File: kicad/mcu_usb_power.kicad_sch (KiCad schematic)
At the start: 41 parts, among them J2 USB4105-GF-A, U7 MCXN947VDFT, U8 PCMF1USB3SZ

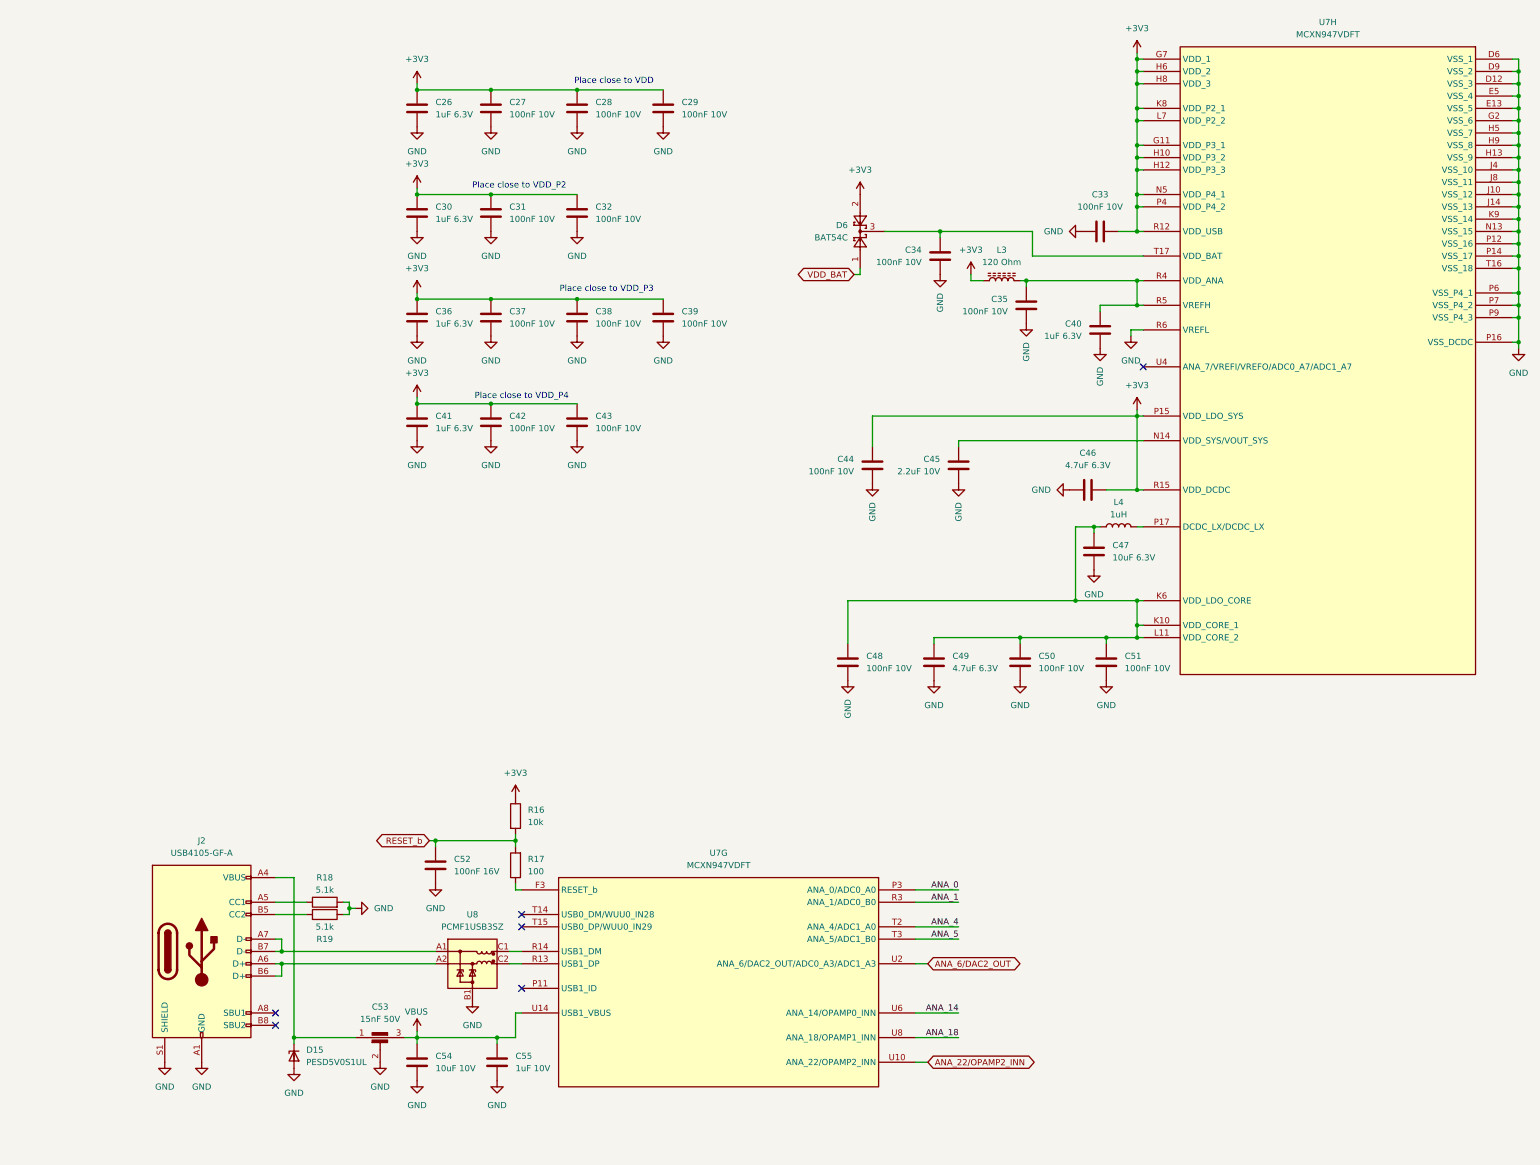
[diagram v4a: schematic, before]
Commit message: Updated schematic after feedback from Jari
- Finished schematic after feedback from Jari. It is at a finished state, can be reviewed by whole team now.
- Layouted MCXN with decoupling caps.
- Layouted Base100-T1 ethernet phy.
- Layouted the power supply a bit.
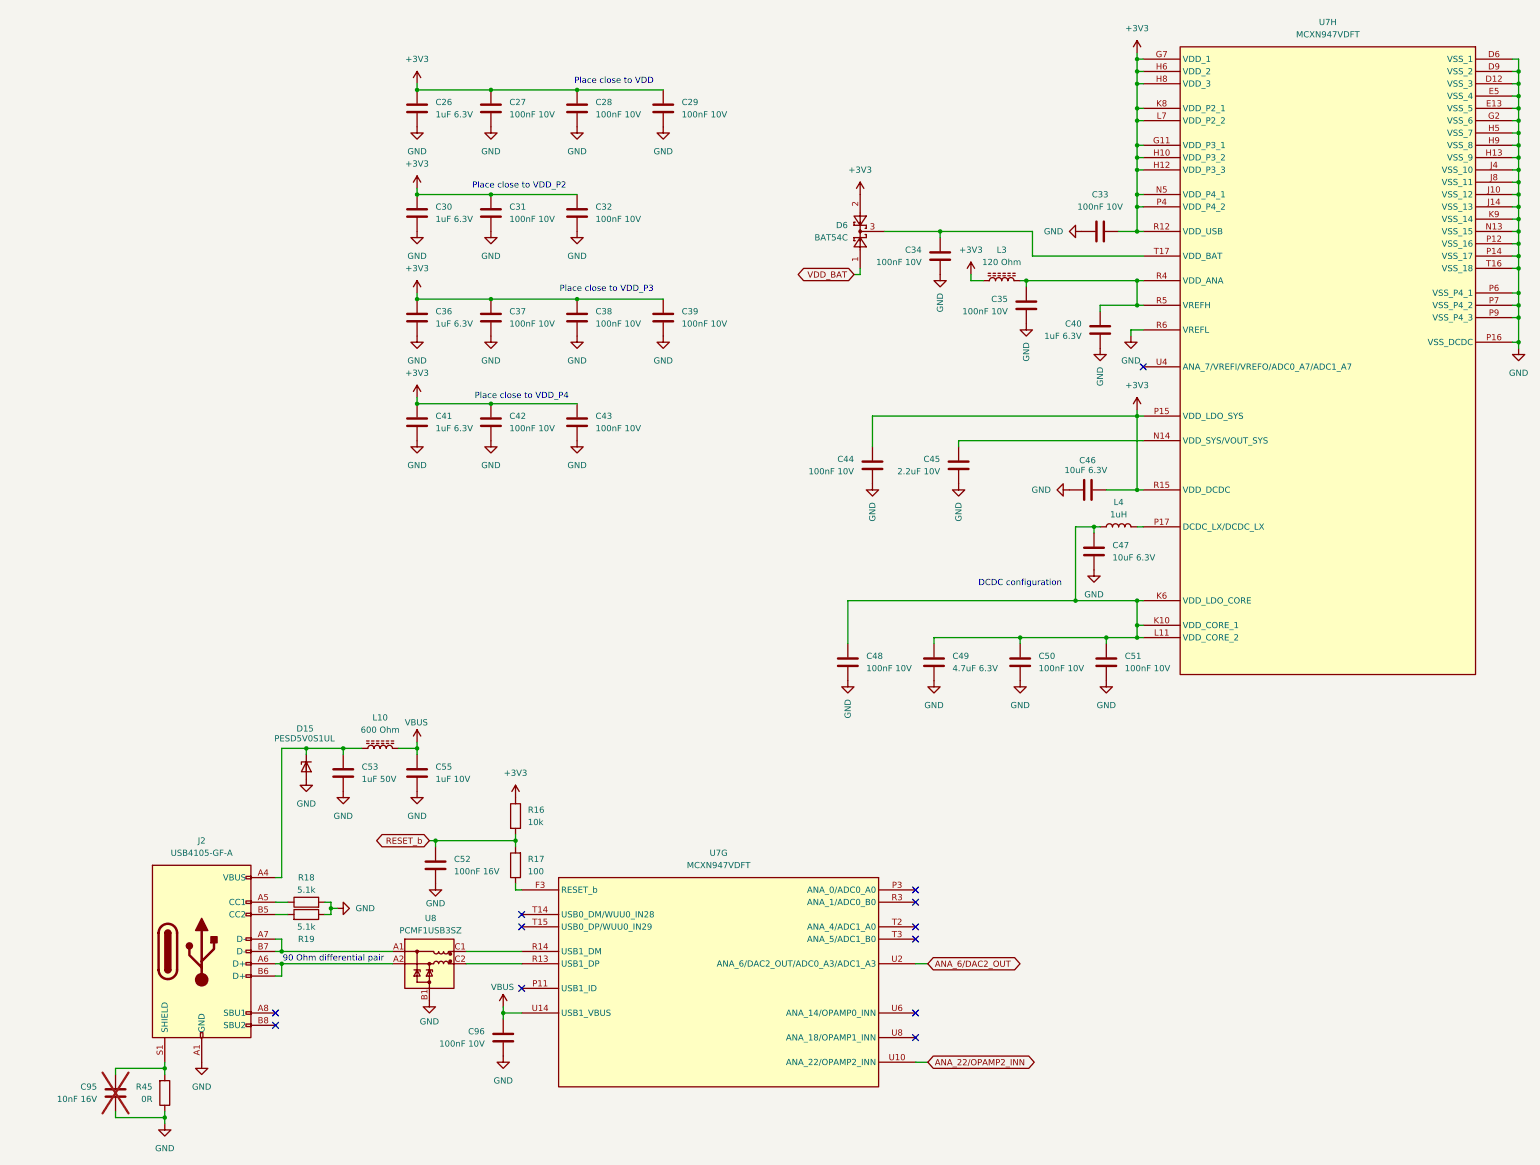
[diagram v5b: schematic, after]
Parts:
- removed C53: 15nF 50V, Capacitors:NFM31HK103R1H3L, symbol Capacitors:NFM31KC153R1H3L
- removed C54: 10uF 10V, Capacitor_SMD:C_0805_2012Metric, symbol Device:C
- added C53: 1uF 50V, Capacitor_SMD:C_0805_2012Metric, symbol Device:C
- added C95: 10nF 16V, symbol Device:C
- added C96: 100nF 10V, Capacitor_SMD:C_0201_0603Metric, symbol Device:C
- added L10: 600 Ohm, Inductor_SMD:L_0402_1005Metric, symbol Device:L_Ferrite
- added R45: 0R, symbol Device:R
- C46: value 4.7uF 6.3V -> 10uF 6.3V; MF Samsung Electro-Mechanics -> Murata Electronics; MFPN CL10B475KQ8NQNC -> GRM188Z71A106KA73D; Supplier PN C107368 -> C2959727
- C55: footprint Capacitor_SMD:C_0603_1608Metric -> Capacitor_SMD:C_0402_1005Metric; MF Samsung Electro-Mechanics -> Murata Electronics; MFPN CL10B105KA8NNNC -> GRM155Z71A105KE01D; Supplier PN C29936 -> C528974
- D15: MF (none) -> Nexperia; MFPN (none) -> PESD5V0S1UL,315; Supplier (none) -> JLCPCB; Supplier PN (none) -> C85402
- J2: MF Korean Hroparts Elec -> Korean Hroparts Elec
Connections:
- net +3V3: now also C46.2; no longer C46.1
- net GND: now also C46.1, C53.2, C95.2, C96.1, R45.1; no longer C46.2, J2.S1 (SHIELD)
- net VBUS: now also C96.2, L10.2
- net at D15.1 (K1), J2.A4 (VBUS), J2.A9 (VBUS)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: now also C53.1, L10.1
- net ANA_0: no longer names the net of U7.P3 (ANA_0/ADC0_A0)
- net ANA_1: no longer names the net of U7.R3 (ANA_1/ADC0_B0)
- net ANA_14: no longer names the net of U7.U6 (ANA_14/OPAMP0_INN)
- net ANA_18: no longer names the net of U7.U8 (ANA_18/OPAMP1_INN)
- net ANA_4: no longer names the net of U7.T2 (ANA_4/ADC1_A0)
- net ANA_5: no longer names the net of U7.T3 (ANA_5/ADC1_B0)
- new net: C95.1, J2.S1 (SHIELD), R45.2
- no-connect marks 6 -> 12
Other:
- note added: "90 Ohm differential pair"
- note added: "DCDC configuration"
- title: MR-MCXN-T1 Sensor hub -> MR-MCXN-T1 Sensor Node
- moved on the sheet: C55, D15, R18, R19, U8

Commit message: Finished schematic. Completed power and ENET phy layout.
Layouted power supply and ethernet phy around input connector.
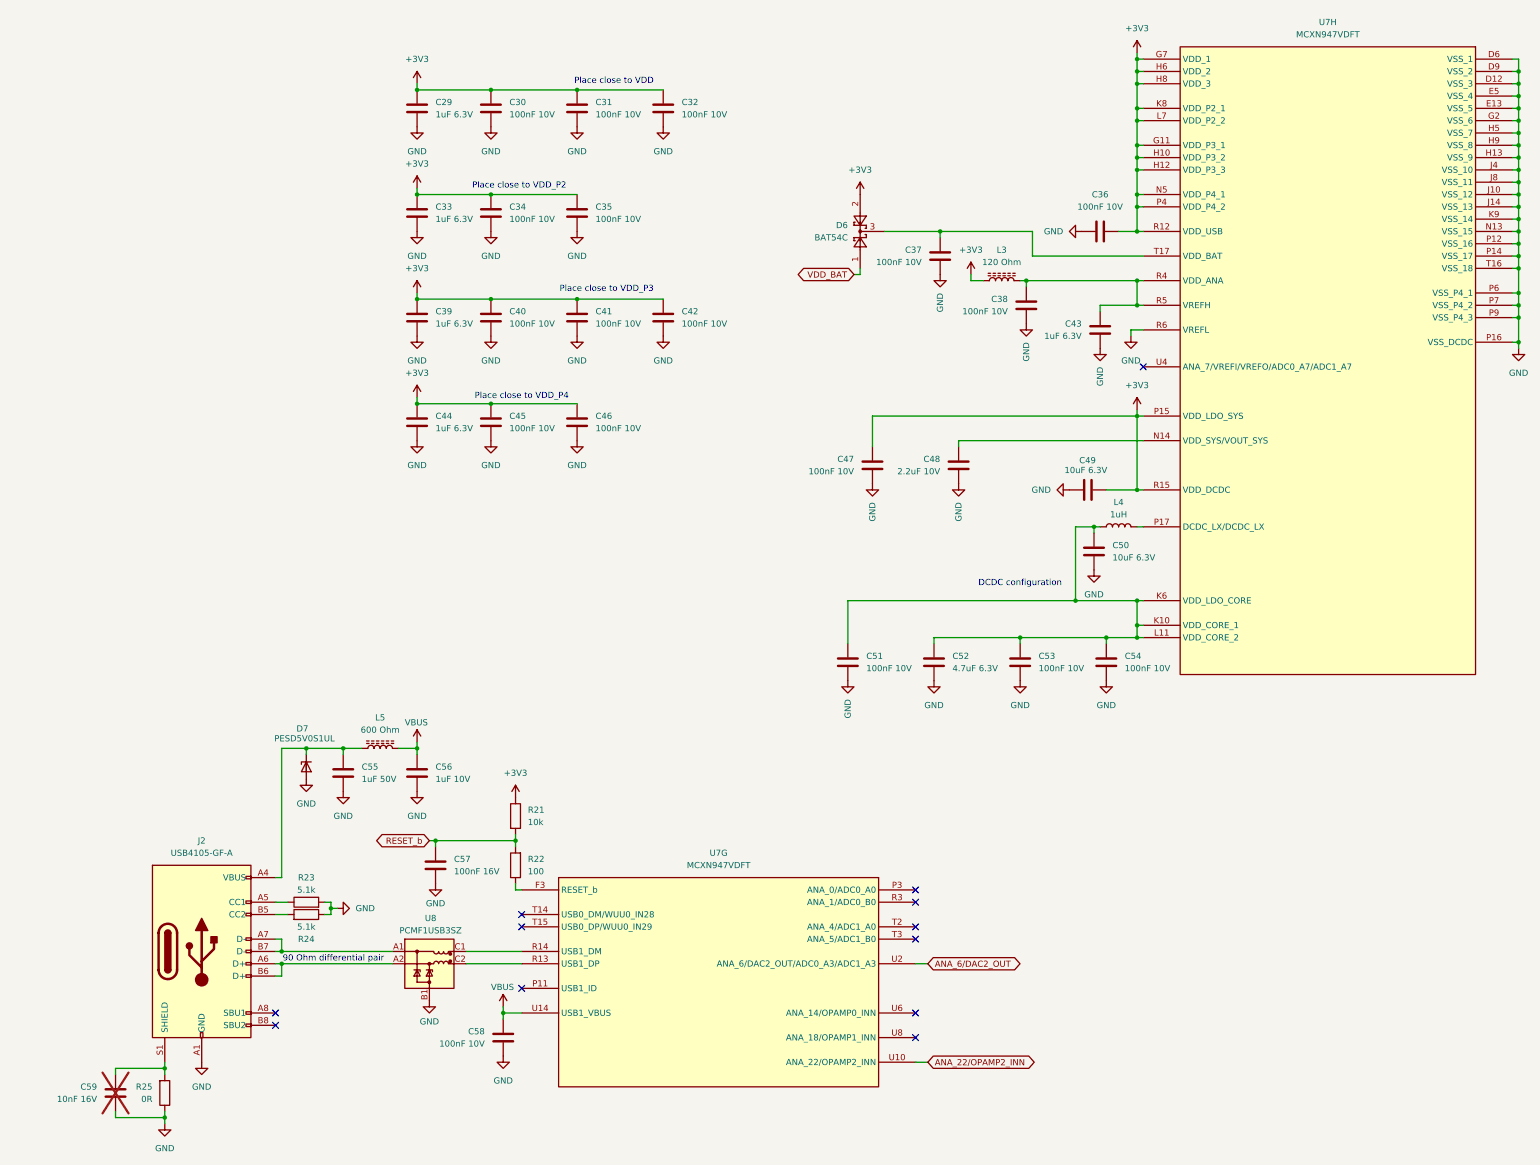
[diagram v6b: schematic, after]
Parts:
- C59: renamed from C95; footprint (none) -> Capacitor_SMD:C_0402_1005Metric; MF (none) -> Murata Electronics; MFPN (none) -> GRM155R71H103KA88D; Supplier (none) -> JLCPCB; Supplier PN (none) -> C77019
- R25: renamed from R45; footprint (none) -> Resistor_SMD:R_0402_1005Metric; MF (none) -> YAGEO; MFPN (none) -> RC0402JR-070RL; Supplier (none) -> JLCPCB; Supplier PN (none) -> C60485
- renumbered C26 to C29, C27 to C30, C28 to C31, C29 to C32, C30 to C33, C31 to C34, C32 to C35, C33 to C36, C34 to C37, C35 to C38, C36 to C39, C37 to C40, C38 to C41, C39 to C42, C40 to C43, C41 to C44, C42 to C45, C43 to C46, C44 to C47, C45 to C48, C46 to C49, C47 to C50, C48 to C51, C49 to C52, C50 to C53, C51 to C54, C53 to C55, C55 to C56, C52 to C57, C96 to C58, D15 to D7, L10 to L5, R16 to R21, R17 to R22, R18 to R23, R19 to R24

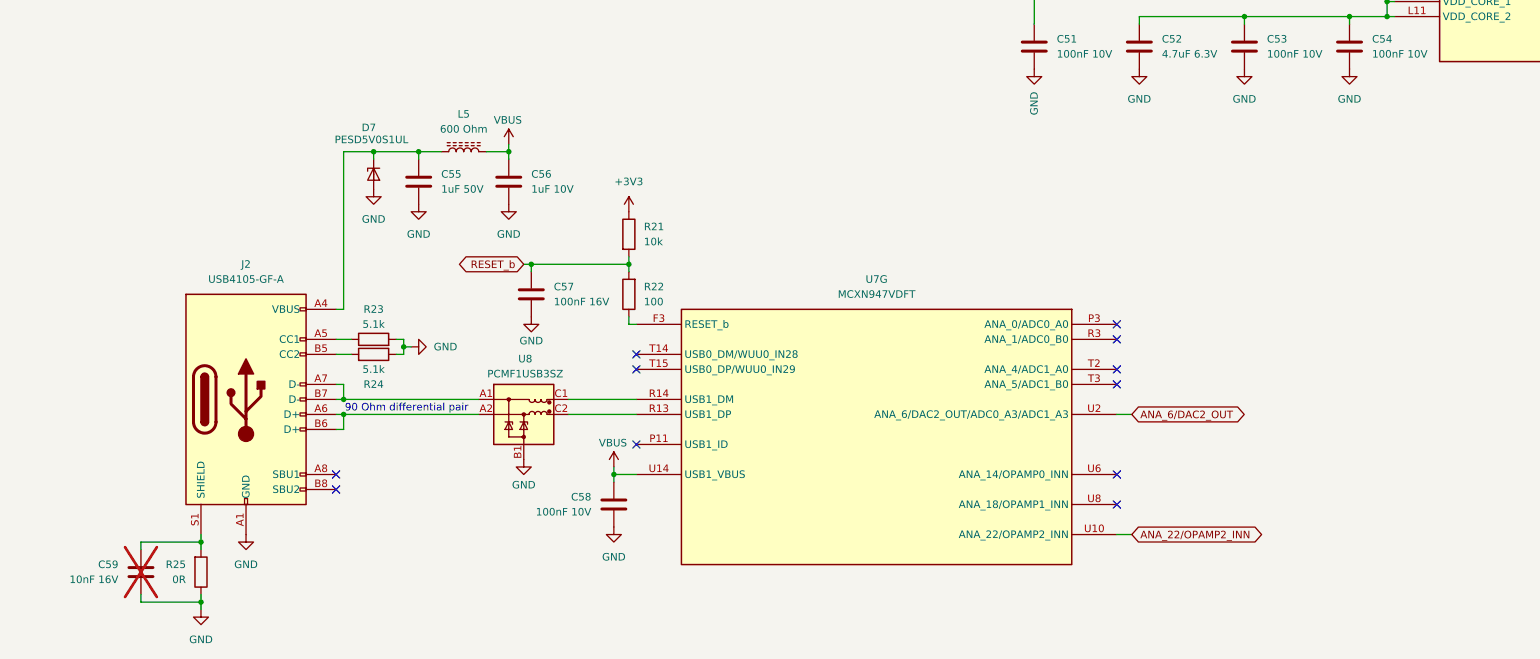
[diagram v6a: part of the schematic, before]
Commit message: Updated PCB layout
Implemented feedback:
- Placed ENET LEDs next to each other
- Added solder pads to output of RGB LED
- Made hole to hole distance in X-axis to 30.5mm
- Placed IMU a bit closer to the middle to still comply to the design rules by TDK.
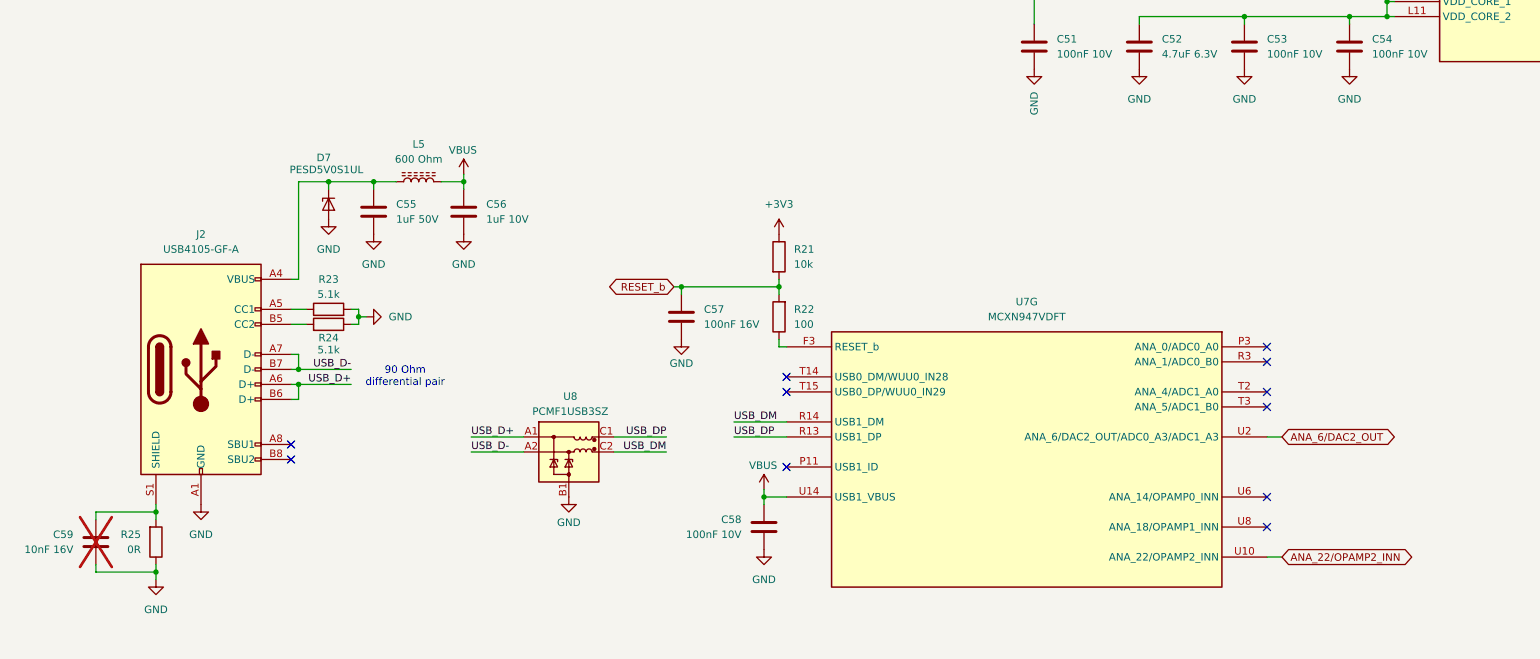
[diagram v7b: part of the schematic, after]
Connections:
- net USB_DM: now reaches U8.C2 (CH1_OUT-)
- net USB_DM: now also U7.R14 (USB1_DM); no longer U7.R13 (USB1_DP)
- net USB_DP: now reaches U8.C1 (CH1_OUT+)
- net USB_DP: now also U7.R13 (USB1_DP); no longer U7.R14 (USB1_DM)
- net USB_D-: now reaches J2.A7 (D-), J2.B7 (D-)
- net USB_D-: now also U8.A2 (CH1_IN-); no longer U8.A1 (CH1_IN+)
- net USB_D+: now reaches J2.A6 (D+), J2.B6 (D+)
- net USB_D+: now also U8.A1 (CH1_IN+); no longer U8.A2 (CH1_IN-)
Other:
- moved on the sheet: C55, C56, C57, C58, C59, D7, J2, L5, R21, R22, R23, R24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

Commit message: Updated layout and BOM
- Flipped Magnetometer so it is aligned with the axis of the IMU.
- Updated BOM so all parts can be sourced from DigiKey. Also added a row for JLCPCB part numbers if applicable.
- Replaced ISP button with the NanoT160AS. Added "ISP" in silkscreen at that button.
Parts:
- C29, C33, C39, C43, C44: DigiKey (none) -> 490-10024-1-ND; JLCPCB (none) -> C88945; Supplier JLCPCB -> (none); Supplier PN C88945 -> (none)
- C30, C31, C32, C34, C35, C36, C37, C38, C40, C41, C42, C45, C46, C47, C51, C53, C54, C58: DigiKey (none) -> 490-GRM033Z71A104KE14DCT-ND; JLCPCB (none) -> C161494; MF Murata Electronics -> Murata Electronics; Supplier JLCPCB -> (none); Supplier PN C161494 -> (none)
- C48: DigiKey (none) -> 490-GRM155Z71A225KE44DCT-ND; JLCPCB (none) -> -; Supplier DigiKey -> (none); Supplier PN 490-GRM155Z71A225KE44DCT-ND -> (none)
- C49, C50: DigiKey (none) -> 490-GRM188Z71A106KA73DCT-ND; JLCPCB (none) -> C2959727; Supplier JLCPCB -> (none); Supplier PN C2959727 -> (none)
- C52: DigiKey (none) -> 490-GRM188Z71A475KE15DCT-ND; JLCPCB (none) -> C913474; MF Samsung Electro-Mechanics -> Murata Electronics; MFPN CL10B475KQ8NQNC -> GRM188Z71A475KE15D; Supplier JLCPCB -> (none); Supplier PN C107368 -> (none)
- C55: JLCPCB (none) -> C77083; Supplier JLCPCB -> (none); Supplier PN C77083 -> (none)
- C56: DigiKey (none) -> 490-GRM155Z71A105KE01DCT-ND; JLCPCB (none) -> C528974; Supplier JLCPCB -> (none); Supplier PN C528974 -> (none)
- C57: DigiKey (none) -> 490-3261-1-ND; JLCPCB (none) -> C71629; MF Samsung Electro-Mechanics -> Murata Electronics; MFPN CL05B104KO5NNNC -> GRM155R71C104KA88D; Supplier JLCPCB -> (none); Supplier PN C1525 -> (none)
- C59: Supplier JLCPCB -> (none); Supplier PN C77019 -> (none)
- D6: DigiKey (none) -> 1727-2902-1-ND; JLCPCB (none) -> C37704; Supplier JLCPCB -> (none); Supplier PN C37704 -> (none)
- D7: DigiKey (none) -> 1727-4189-1-ND; JLCPCB (none) -> C85402; Supplier JLCPCB -> (none); Supplier PN C85402 -> (none)
- J2: DigiKey (none) -> 2073-USB4105-GF-ACT-ND; JLCPCB (none) -> C165948; MF Korean Hroparts Elec -> GCT; MFPN TYPE-C-31-M-12 -> USB4105-GF-A; Supplier JLCPCB -> (none); Supplier PN C165948 -> (none)
- L3: DigiKey (none) -> 490-1005-1-ND; JLCPCB (none) -> C85812; Supplier JLCPCB -> (none); Supplier PN C85812 -> (none)
- L4: DigiKey (none) -> 587-5973-1-ND; JLCPCB (none) -> C5669778; Supplier JLCPCB -> (none); Supplier PN C5669778 -> (none)
- L5: DigiKey (none) -> 490-1006-1-ND; JLCPCB (none) -> C76884; Supplier JLCPCB -> (none); Supplier PN C76884 -> (none)
- R21: DigiKey (none) -> YAG3436CT-ND; JLCPCB (none) -> C144807; MF UNI-ROYAL(Uniroyal Elec) -> YAGEO; MFPN 0402WGF1002TCE -> AC0402FR-0710KL; Supplier JLCPCB -> (none); Supplier PN C25744 -> (none)
- R22: DigiKey (none) -> YAG3561CT-ND; JLCPCB (none) -> C125923; MF UNI-ROYAL(Uniroyal Elec) -> YAGEO; MFPN 0603WAF1000T5E -> AC0603FR-07100RL; Supplier JLCPCB -> (none); Supplier PN C22775 -> (none)
- R23, R24: DigiKey (none) -> YAG3503CT-ND; JLCPCB (none) -> C144745; MF UNI-ROYAL(Uniroyal Elec) -> YAGEO; MFPN 0402WGF5101TCE -> AC0402FR-075K1L; Supplier JLCPCB -> (none); Supplier PN C25905 -> (none)
- R25: DigiKey (none) -> 311-0.0JRCT-ND; JLCPCB (none) -> C60485; Supplier JLCPCB -> (none); Supplier PN C60485 -> (none)
- U7: DigiKey (none) -> 568-MCXN947VDFT-ND; JLCPCB (none) -> -; Supplier DigiKey -> (none); Supplier PN 568-MCXN947VDFT-ND -> (none)
- U8: DigiKey (none) -> 1727-2508-1-ND; JLCPCB (none) -> -; Supplier DigiKey -> (none); Supplier PN 1727-2508-1-ND -> (none)
